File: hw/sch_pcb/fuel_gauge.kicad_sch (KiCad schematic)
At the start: 36 parts, among them J10 HEADER_2x01_PARALLEL, J11 HEADER_1x02, Q2 AP2305AGN-HF-3, Q3 DMTH3002LPS, Q5 DMTH3002LPS, SW1 SW_Push, SW2 SW_Push, U3 BQ40z50-R2

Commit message: Fix whitespaces around USTids.
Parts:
- C17, C18, C21: UST_ID 5c70984712875079b91f8b4c -> 5c70984712875079b91f8b4c
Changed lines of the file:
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@@
 			)
 		)
-		(property "UST_ID" " 5c70984712875079b91f8b4c "
+		(property "UST_ID" "5c70984712875079b91f8b4c"
 			(at 74.93 132.08 0)
 			(effects
@@
 			)
 		)
-		(property "UST_ID" " 5c70984712875079b91f8b4c "
+		(property "UST_ID" "5c70984712875079b91f8b4c"
 			(at 82.55 114.3 0)
 			(effects
@@
 			)
 		)
-		(property "UST_ID" " 5c70984712875079b91f8b4c "
+		(property "UST_ID" "5c70984712875079b91f8b4c"
 			(at 82.55 106.68 0)
 			(effects

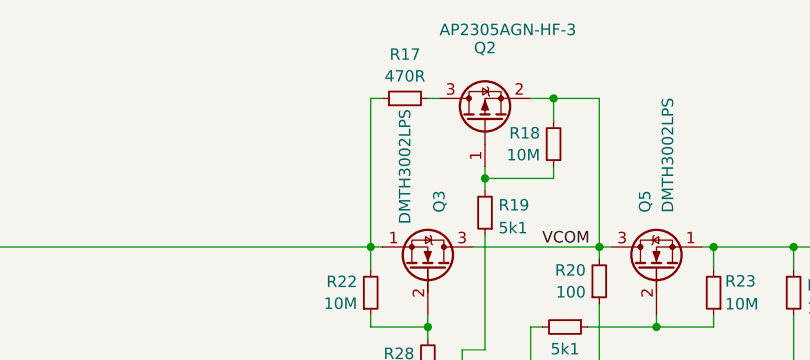
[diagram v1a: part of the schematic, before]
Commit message: Fix components identification.
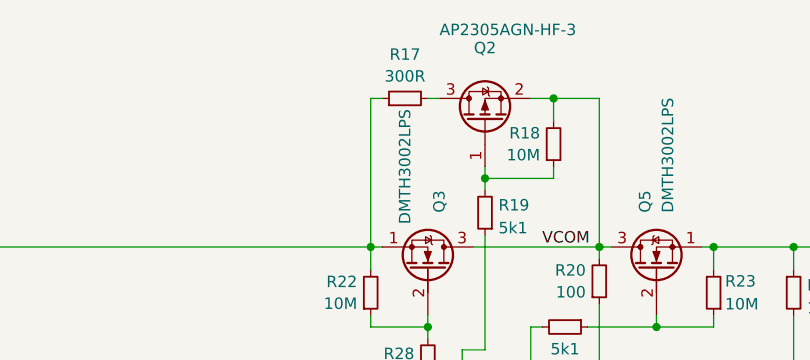
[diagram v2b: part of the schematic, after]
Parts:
- R17: value 470R -> 300R; UST_ID 60be2ed51287500165e6c1cd -> 5c70984712875079b91f8ab8
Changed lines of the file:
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@@
 			)
 		)
-		(property "Value" "470R"
+		(property "Value" "300R"
 			(at 110.49 47.0732 90)
 			(effects
@@
 			)
 		)
-		(property "UST_ID" "60be2ed51287500165e6c1cd"
+		(property "UST_ID" "5c70984712875079b91f8ab8"
 			(at 110.49 49.53 0)
 			(effects
